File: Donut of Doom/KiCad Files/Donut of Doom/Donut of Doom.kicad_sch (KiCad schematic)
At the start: 30 parts, among them Q1 Q_NMOS_GSD

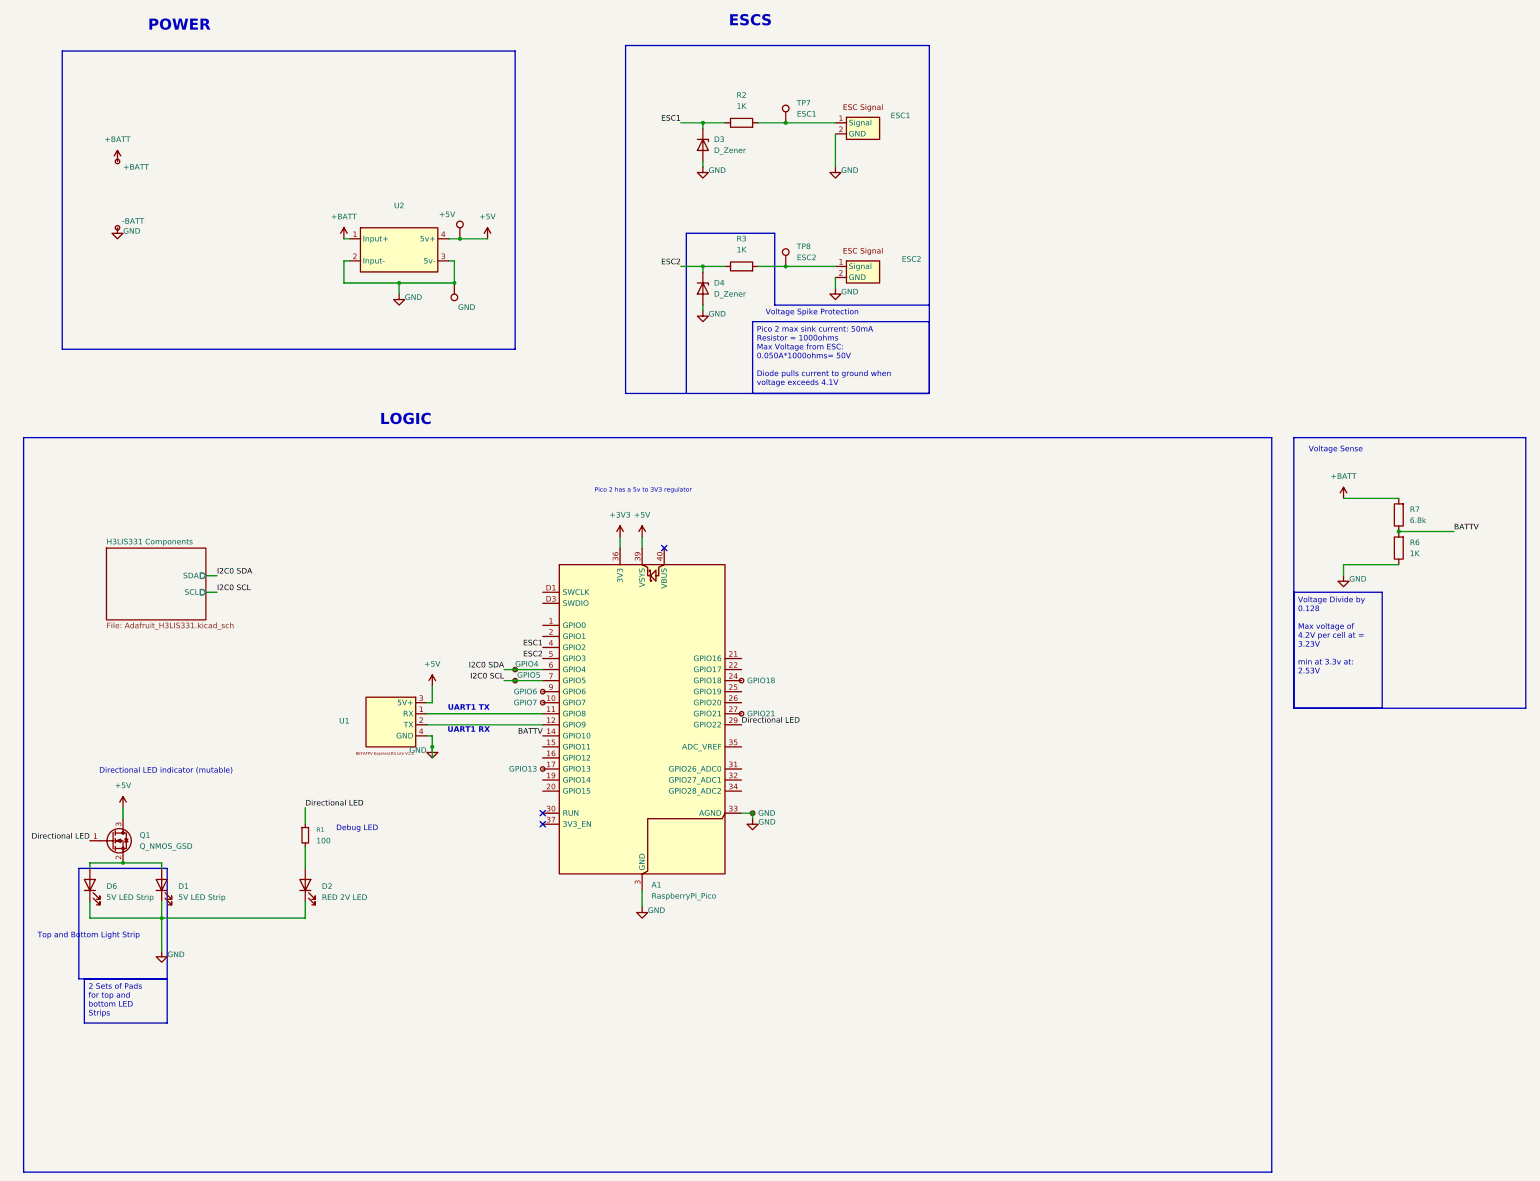
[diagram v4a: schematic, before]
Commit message: Added 2nd accel, fixed mosfet, added more GND pads
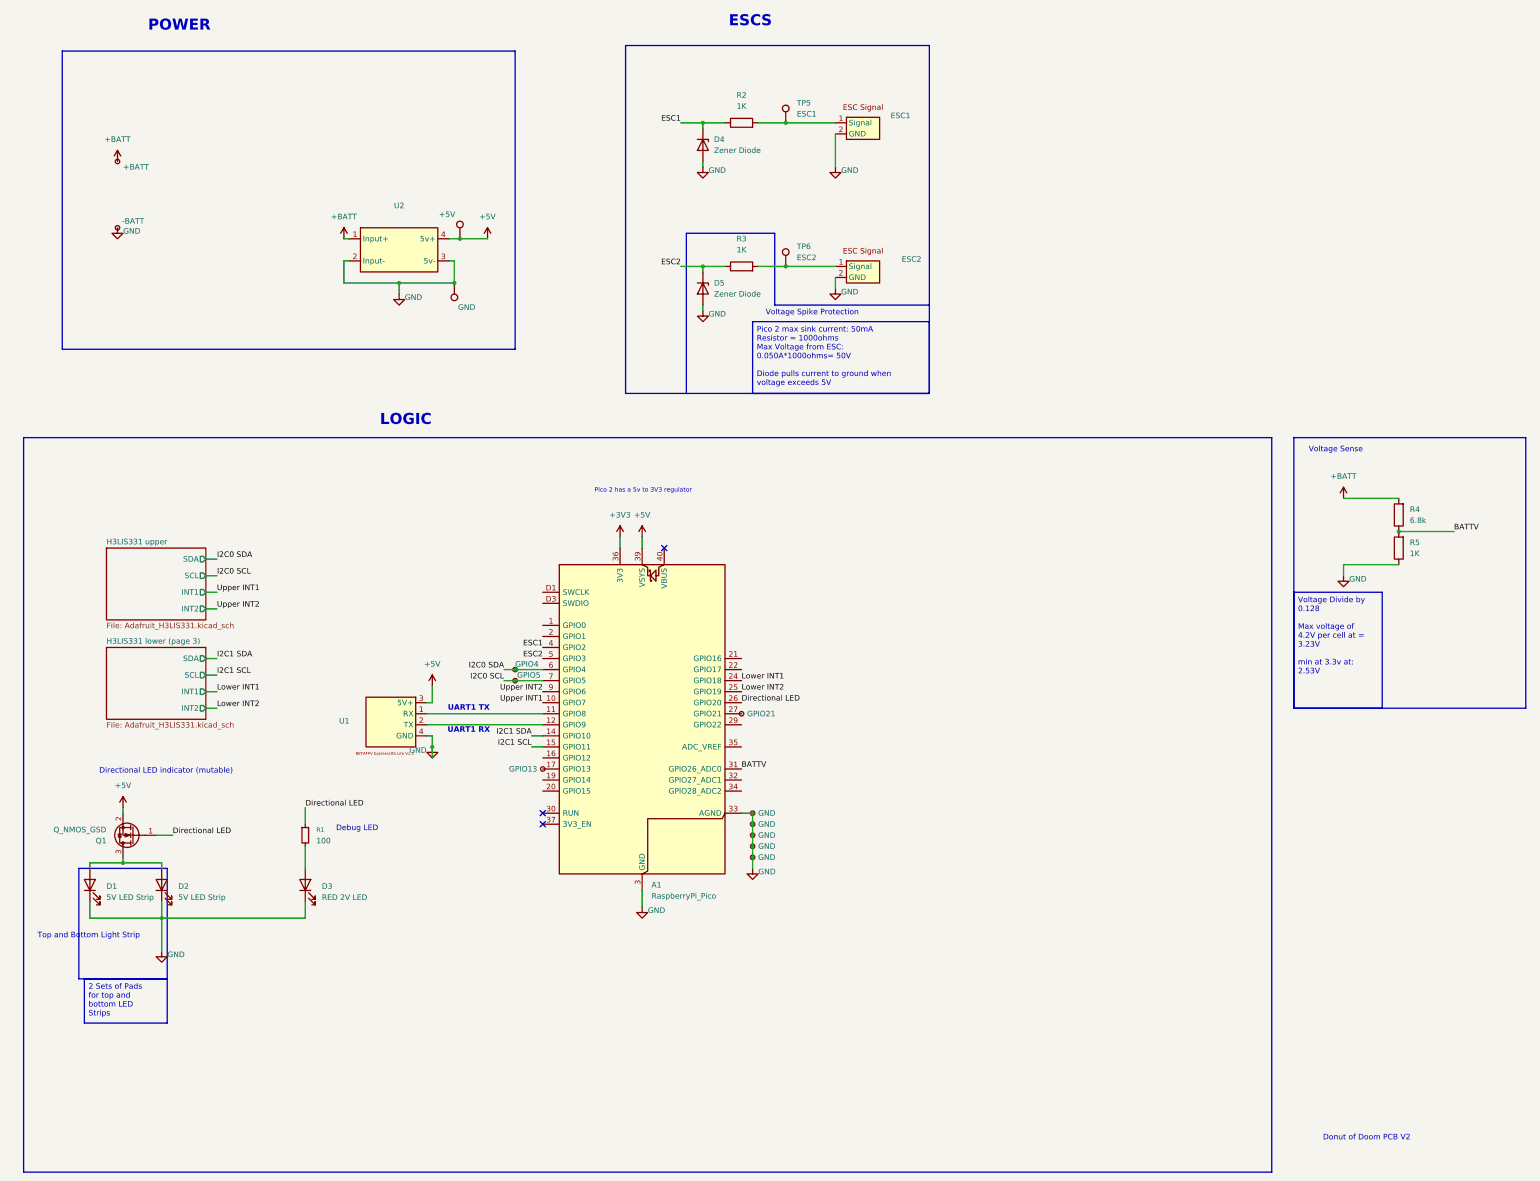
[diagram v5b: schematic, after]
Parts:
- removed EX1: GPIO6, Battlebots:Pico_pth_pad, symbol Connector:TestPoint_Small
- removed EX2: GPIO7, Battlebots:Pico_pth_pad, symbol Connector:TestPoint_Small
- removed EX4: GPIO18, Battlebots:Pico_pth_pad, symbol Connector:TestPoint_Small
- added EX10, EX11, EX12, EX9: GND, Battlebots:Pico_pth_GND, symbol Connector:TestPoint_Small
- D4: renamed from D3; value D_Zener -> Zener Diode
- D5: renamed from D4; value D_Zener -> Zener Diode
- renumbered D6 to D1, D1 to D2, D2 to D3, EX5 to EX1, EX6 to EX2, EX3 to EX5, R7 to R4, R6 to R5, TP5 to TP1, TP6 to TP2, TP4 to TP3, TP3 to TP4, TP7 to TP5, TP8 to TP6
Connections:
- net +5V: now also Q1.2 (S); no longer Q1.3 (D)
- net BATTV: now also A1.31 (GPIO26_ADC0); no longer A1.14 (GPIO10)
- net Directional LED: now also A1.26 (GPIO20); no longer A1.29 (GPIO22)
- net GND: now also EX10.1, EX11.1, EX12.1, EX9.1
- net Upper INT1: now reaches A1.10 (GPIO7)
- net I2C1 SCL: now reaches A1.15 (GPIO11)
- net Lower INT1: now reaches A1.24 (GPIO18)
- net Lower INT2: now reaches A1.25 (GPIO19)
- net Upper INT2: now reaches A1.9 (GPIO6)
- net at D1.2 (A), D2.2 (A): now also Q1.3 (D); no longer Q1.2 (S)
- new net I2C1 SDA: A1.14 (GPIO10)
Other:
- sheet H3LIS331 Components renamed H3LIS331 upper
- added sheet H3LIS331 lower (page 3) (Adafruit_H3LIS331.kicad_sch)
- sheet H3LIS331 upper ports: added INT1, INT2; removed none
- note added: "Donut of Doom PCB V2"
- moved on the sheet: Q1

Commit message: V3 First rev finished
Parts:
- removed D3: RED 2V LED, LED_SMD:LED_0603_1608Metric_Pad1.05x0.95mm_HandSolder, symbol Device:LED
- removed EX10: GND, Battlebots:Pico_pth_GND, symbol Connector:TestPoint_Small
- removed EX7: GPIO21, Battlebots:Pico_pth_pad, symbol Connector:TestPoint_Small
- removed R1: 100, Resistor_SMD:R_0603_1608Metric_Pad0.98x0.95mm_HandSolder, symbol Device:R_Small
- added H1, H2: MountingHole_Pad, MountingHole:MountingHole_2.2mm_M2_DIN965_Pad, symbol Mechanical:MountingHole_Pad
- added JP1: Solder_Jumper, Jumper:SolderJumper-3_P1.3mm_Open_RoundedPad1.0x1.5mm_NumberLabels, symbol Jumper:SolderJumper_3_Open
- ESC1, ESC2, U1, U2: value ~ -> (none)
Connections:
- net +5V: now also JP1.3 (B); no longer Q1.2 (S)
- net +BATT: now also JP1.1 (A)
- net GND: now also Q1.2 (S), H1.1, H2.1; no longer D1.1 (K), D2.1 (K)
- net at D1.2 (A), D2.2 (A): now also JP1.2 (C); no longer Q1.3 (D)
- new net: D1.1 (K), D2.1 (K), Q1.3 (D)
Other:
- note removed: "Debug LED"
- note removed: "Directional LED indicator (mutable)"
- moved on the sheet: D1, D2
